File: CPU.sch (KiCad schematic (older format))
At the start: 13 parts, among them P8 SWD, U1 STM32F40X_LQFP64, Y1 Crystal

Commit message: - removed lots of unused circuitry - implemented new DMOS power stage - power supplies still missing - removed rescue lib and fixed referenced
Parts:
- removed C17, C22: 15p, Capacitor_SMD:C_0805_2012Metric, symbol Revolter-rescue:C-RESCUE-BLDC_4
- removed U1: STM32F40X_LQFP64, Package_QFP:LQFP-64_10x10mm_P0.5mm, symbol Revolter-rescue:STM32F40X_LQFP64
- removed Y1: Crystal, Crystal:Crystal_HC49-U_Vertical, symbol Device:Crystal
- added C1, C3: 15p, symbol Device:C_Small
- added C4: 1u, Capacitor_SMD:C_0805_2012Metric, symbol Device:C
- added L1: 100u, symbol pspice:INDUCTOR
- added U1: STM32F405RGTx, Package_QFP:LQFP-64_10x10mm_P0.5mm, symbol MCU_ST_STM32F4:STM32F405RGTx
- added Y1: 8MHz, symbol Device:Crystal_Small
- C18, C19, C20, C21, C23, C24, C25, C26: symbol Revolter-rescue:C-RESCUE-BLDC_4 -> Device:C
- P8: symbol Revolter-rescue:CONN_6 -> Connector_Generic:Conn_01x06
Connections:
- net labels added: CURRENT_U, CURRENT_V, CURRENT_W, HALL_U, HALL_V, HALL_W, HU, HV, HW, LU, LV, LW, VOLTAGE_U, VOLTAGE_V, VOLTAGE_W
- net labels removed: CURRENT_1, CURRENT_2, CURRENT_3, H1, H2, H3, HALL_1, HALL_2, HALL_3, L1, L2, L3, SERVO, VOLTAGE_1, VOLTAGE_2, VOLTAGE_3
- wire segments 69 -> 19
- no-connect marks 17 -> 20
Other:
- note removed: "Bypass, place next to VDD pins"
- note removed: "Required for USB\nto work"
- note removed: "Reset pin internally\npulled up"

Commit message: - fixed ACS730 pin issue - added power supplies - added footprint library - added footprint for IRSM005
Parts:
- removed Y1: 8MHz, symbol Device:Crystal_Small
- added Y1: 8MHz, Crystal:Crystal_SMD_3225-4Pin_3.2x2.5mm, symbol Device:Crystal_GND24
- C1, C3: footprint (none) -> Capacitor_SMD:C_0805_2012Metric
- L1: footprint (none) -> Inductor_SMD:L_0805_2012Metric
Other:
- moved on the sheet: C1, C3
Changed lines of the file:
@@
 F 0 "L1" V 5954 1328 50  0000 L CNN
 F 1 "100u" V 6045 1328 50  0000 L CNN
-F 2 "" H 6000 1250 50  0001 C CNN
+F 2 "Inductor_SMD:L_0805_2012Metric" H 6000 1250 50  0001 C CNN
 F 3 "~" H 6000 1250 50  0001 C CNN
 	1    6000 1250
@@
 	4900 1700 4750 1700
 $Comp
-L Device:Crystal_Small Y1
-U 1 1 5EE66624
-P 4000 2900
-F 0 "Y1" H 4000 3125 50  0000 C CNN
-F 1 "8MHz" H 4000 3034 50  0000 C CNN
-F 2 "" H 4000 2900 50  0001 C CNN
-F 3 "~" H 4000 2900 50  0001 C CNN
-	1    4000 2900
-	1    0    0    -1
-$EndComp
-Wire Wire Line
-	4100 2900 5000 2900
-Wire Wire Line
-	5000 3000 3900 3000
-Wire Wire Line
-	3900 3000 3900 2900
-$Comp
 L Device:C_Small C1
 U 1 1 5EE68BFE
-P 3900 3150
-F 0 "C1" H 3808 3104 50  0000 R CNN
-F 1 "15p" H 3808 3195 50  0000 R CNN
-F 2 "" H 3900 3150 50  0001 C CNN
-F 3 "~" H 3900 3150 50  0001 C CNN
-	1    3900 3150
+P 3750 3200
+F 0 "C1" H 3658 3154 50  0000 R CNN
+F 1 "15p" H 3658 3245 50  0000 R CNN
+F 2 "Capacitor_SMD:C_0805_2012Metric" H 3750 3200 50  0001 C CNN
+F 3 "~" H 3750 3200 50  0001 C CNN
+	1    3750 3200
 	1    0    0    1
 $EndComp
@@
 L Device:C_Small C3
 U 1 1 5EE6B932
-P 4100 3150
-F 0 "C3" H 4008 3196 50  0000 R CNN
-F 1 "15p" H 4008 3105 50  0000 R CNN
-F 2 "" H 4100 3150 50  0001 C CNN
-F 3 "~" H 4100 3150 50  0001 C CNN
-	1    4100 3150
+P 4050 3200
+F 0 "C3" H 3958 3246 50  0000 R CNN
+F 1 "15p" H 3958 3155 50  0000 R CNN
+F 2 "Capacitor_SMD:C_0805_2012Metric" H 4050 3200 50  0001 C CNN
+F 3 "~" H 4050 3200 50  0001 C CNN
+	1    4050 3200
 	-1   0    0    -1
 $EndComp
 Wire Wire Line
-	4100 3050 4100 2900
-Connection ~ 4100 2900
-Wire Wire Line
-	3900 3000 3900 3050
-Connection ~ 3900 3000
+	4050 3100 4050 2900
+Wire Wire Line
+	3750 3000 3750 3100
 $Comp
 L power:GND #PWR0114
 U 1 1 5EE6D37C
-P 3900 3250
-F 0 "#PWR0114" H 3900 3000 50  0001 C CNN
-F 1 "GND" H 3905 3077 50  0000 C CNN
-F 2 "" H 3900 3250 50  0001 C CNN
-F 3 "" H 3900 3250 50  0001 C CNN
-	1    3900 3250
+P 3750 3300
+F 0 "#PWR0114" H 3750 3050 50  0001 C CNN
+F 1 "GND" H 3755 3127 50  0000 C CNN
+F 2 "" H 3750 3300 50  0001 C CNN
+F 3 "" H 3750 3300 50  0001 C CNN
+	1    3750 3300
 	1    0    0    -1
 $EndComp
@@
 L power:GND #PWR0115
 U 1 1 5EE6E0B7
-P 4100 3250
-F 0 "#PWR0115" H 4100 3000 50  0001 C CNN
-F 1 "GND" H 4105 3077 50  0000 C CNN
-F 2 "" H 4100 3250 50  0001 C CNN
-F 3 "" H 4100 3250 50  0001 C CNN
-	1    4100 3250
+P 4050 3300
+F 0 "#PWR0115" H 4050 3050 50  0001 C CNN
+F 1 "GND" H 4055 3127 50  0000 C CNN
+F 2 "" H 4050 3300 50  0001 C CNN
+F 3 "" H 4050 3300 50  0001 C CNN
+	1    4050 3300
 	1    0    0    -1
 $EndComp
@@
 NoConn ~ 5000 4900
 NoConn ~ 5000 3200
+$Comp
+L Device:Crystal_GND24 Y1
+U 1 1 5EF3EE13
+P 3900 2900
+F 0 "Y1" H 4094 2946 50  0000 L CNN
+F 1 "8MHz" H 4094 2855 50  0000 L CNN
+F 2 "Crystal:Crystal_SMD_3225-4Pin_3.2x2.5mm" H 3900 2900 50  0001 C CNN
+F 3 "~" H 3900 2900 50  0001 C CNN
+	1    3900 2900
+	1    0    0    -1
+$EndComp
+Wire Wire Line
+	4050 2900 5000 2900
+Wire Wire Line
+	5000 3000 3750 3000
+Wire Wire Line
+	3750 3000 3750 2900
+Connection ~ 3750 3000
+Connection ~ 4050 2900
+$Comp
+L power:GND #PWR0177
+U 1 1 5EF48D07
+P 3900 3100
+F 0 "#PWR0177" H 3900 2850 50  0001 C CNN
+F 1 "GND" H 3905 2927 50  0000 C CNN
+F 2 "" H 3900 3100 50  0001 C CNN
+F 3 "" H 3900 3100 50  0001 C CNN
+	1    3900 3100
+	1    0    0    -1
+$EndComp
+$Comp
+L power:GND #PWR0178
+U 1 1 5EF4921F
+P 3900 2700
+F 0 "#PWR0178" H 3900 2450 50  0001 C CNN
+F 1 "GND" H 3905 2527 50  0000 C CNN
+F 2 "" H 3900 2700 50  0001 C CNN
+F 3 "" H 3900 2700 50  0001 C CNN
+	1    3900 2700
+	-1   0    0    1
+$EndComp
 $EndSCHEMATC

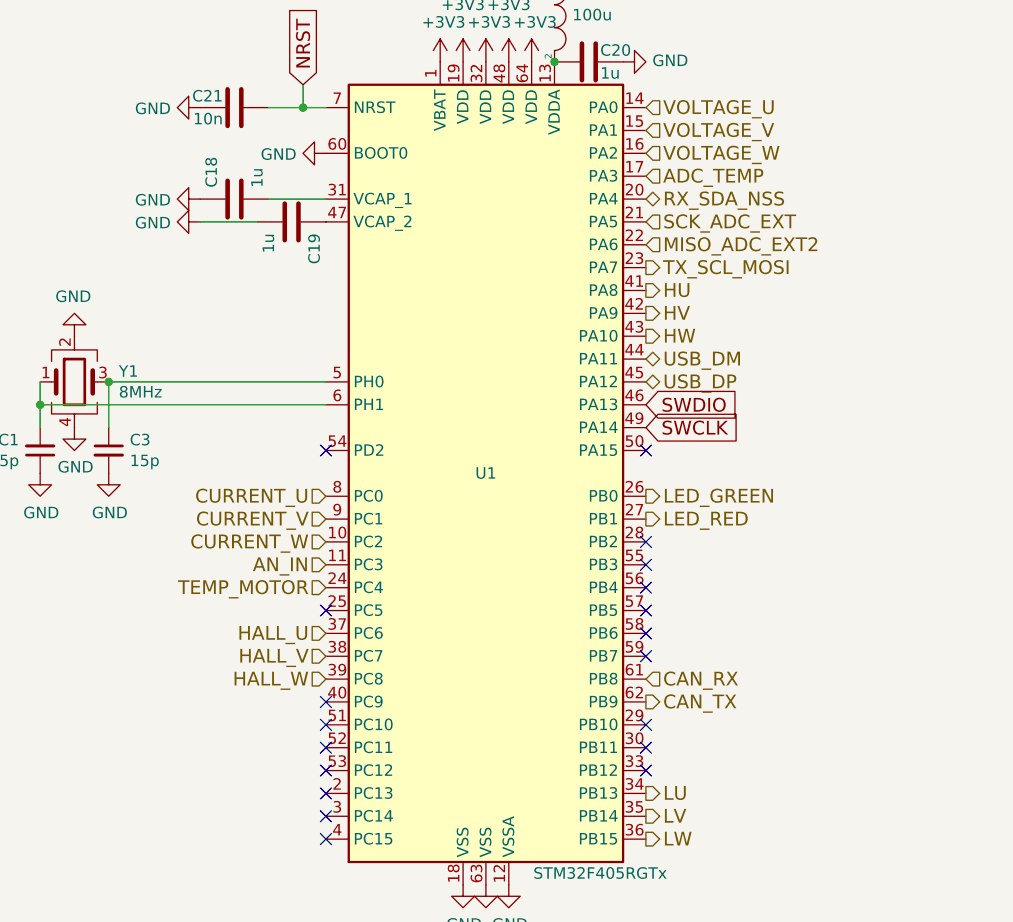
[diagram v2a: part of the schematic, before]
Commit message: - added temp sensors and fan/pump outputs - made footprint selection
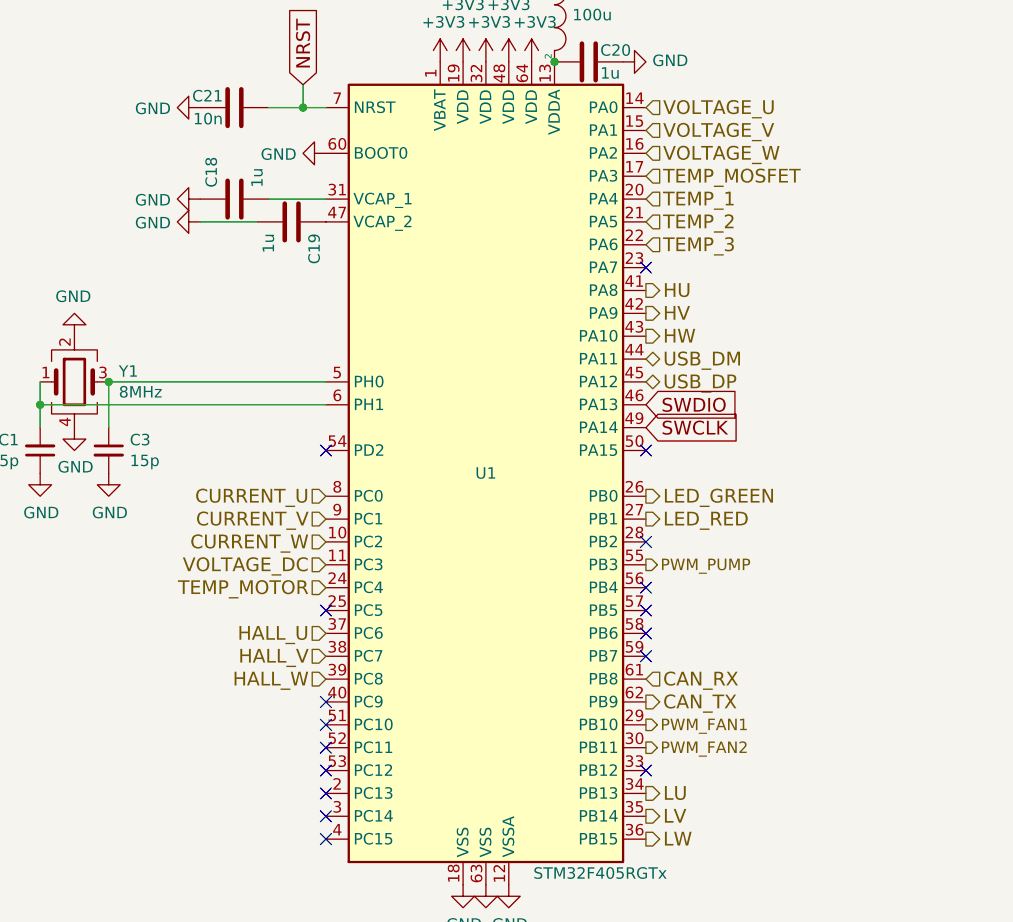
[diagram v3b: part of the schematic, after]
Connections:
- net labels added: PWM_FAN1, PWM_FAN2, PWM_PUMP, TEMP_1, TEMP_2, TEMP_3, TEMP_MOSFET, VOLTAGE_DC
- net labels removed: ADC_TEMP, AN_IN, MISO_ADC_EXT2, RX_SDA_NSS, SCK_ADC_EXT, TX_SCL_MOSI
- no-connect marks 20 -> 18
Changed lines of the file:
@@
 $Descr A4 11693 8268
 encoding utf-8
-Sheet 2 4
+Sheet 4 4
 Title "HSWR CPU"
 Date "2017-02-05"
@@
 LU
 Text HLabel 6400 2200 2    60   Input ~ 0
-SCK_ADC_EXT
+TEMP_2
 Text HLabel 6400 2500 2    60   Output ~ 0
 HU
@@
 CURRENT_U
 Text HLabel 5000 3700 0    60   Input ~ 0
-AN_IN
+VOLTAGE_DC
 Wire Notes Line
 	9250 2650 9250 3550
@@
 LED_GREEN
 Text HLabel 6400 2300 2    60   Input ~ 0
-MISO_ADC_EXT2
-Text HLabel 6400 2400 2    60   Output ~ 0
-TX_SCL_MOSI
+TEMP_3
 Text HLabel 6400 2000 2    60   Input ~ 0
-ADC_TEMP
-Text HLabel 6400 2100 2    60   3State ~ 0
-RX_SDA_NSS
+TEMP_MOSFET
+Text HLabel 6400 2100 2    60   Input ~ 0
+TEMP_1
 $Comp
 L power:+3V3 #PWR050
@@
 HALL_W
 $Comp
-L MCU_ST_STM32F4:STM32F405RGTx U1
-U 1 1 5EE38B5C
-P 5700 3300
-F 0 "U1" H 5700 3300 50  0000 C CNN
-F 1 "STM32F405RGTx" H 6200 1550 50  0000 C CNN
-F 2 "Package_QFP:LQFP-64_10x10mm_P0.5mm" H 5100 1600 50  0001 R CNN
-F 3 "http://www.st.com/st-web-ui/static/active/en/resource/technical/document/datasheet/DM00037051.pdf" H 5700 3300 50  0001 C CNN
-	1    5700 3300
-	1    0    0    -1
-$EndComp
-$Comp
 L power:GND #PWR0101
 U 1 1 5EE3F753
@@
 	0    -1   -1   0
 $EndComp
-Connection ~ 6000 1500
 Wire Wire Line
 	4750 2100 5000 2100
@@
 	0    1    1    0
 $EndComp
-NoConn ~ 6400 3700
 NoConn ~ 6400 3800
 NoConn ~ 6400 3900
 NoConn ~ 6400 4000
 NoConn ~ 6400 4100
-NoConn ~ 6400 4400
-NoConn ~ 6400 4500
 NoConn ~ 6400 4600
 NoConn ~ 5000 3900
@@
 	-1   0    0    1
 $EndComp
+Connection ~ 6000 1500
+$Comp
+L MCU_ST_STM32F4:STM32F405RGTx U1
+U 1 1 5EE38B5C
+P 5700 3300
+F 0 "U1" H 5700 3300 50  0000 C CNN
+F 1 "STM32F405RGTx" H 6200 1550 50  0000 C CNN
+F 2 "Package_QFP:LQFP-64_10x10mm_P0.5mm" H 5100 1600 50  0001 R CNN
+F 3 "http://www.st.com/st-web-ui/static/active/en/resource/technical/document/datasheet/DM00037051.pdf" H 5700 3300 50  0001 C CNN
+	1    5700 3300
+	1    0    0    -1
+$EndComp
+Text HLabel 6400 3700 2    50   Output ~ 0
+PWM_PUMP
+NoConn ~ 6400 2400
+Text HLabel 6400 4400 2    50   Output ~ 0
+PWM_FAN1
+Text HLabel 6400 4500 2    50   Output ~ 0
+PWM_FAN2
 $EndSCHEMATC

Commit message: - did most of the layout
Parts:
- removed C26: 1u, Capacitor_SMD:C_0805_2012Metric, symbol Device:C
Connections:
- wire segments 19 -> 17
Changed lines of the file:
@@
 	-1   0    0    1
 $EndComp
-$Comp
-L Device:C C26
-U 1 1 53F7744E
-P 10100 1300
-AR Path="/53F7744E" Ref="C26"  Part="1"
-AR Path="/5899E230/53F7744E" Ref="C26"  Part="1"
-F 0 "C26" H 10150 1400 50  0000 L CNN
-F 1 "1u" H 10150 1200 50  0000 L CNN
-F 2 "Capacitor_SMD:C_0805_2012Metric" H 10100 1300 60  0001 C CNN
-F 3 "" H 10100 1300 60  0001 C CNN
-	1    10100 1300
-	-1   0    0    1
-$EndComp
-Connection ~ 9900 1450
 Connection ~ 9700 1450
 Connection ~ 9700 1150
-Connection ~ 9900 1150
 Wire Wire Line
 	9750 3100 9600 3100
@@
 $EndComp
 Wire Wire Line
-	9900 1450 10100 1450
-Wire Wire Line
 	9500 1450 9700 1450
 Wire Wire Line
 	9500 1150 9700 1150
-Wire Wire Line
-	9900 1150 10100 1150
 Text HLabel 5000 3500 0    60   Input ~ 0
 CURRENT_V

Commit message: - shrink PCB to 50x50mm
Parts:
- removed C21: 10n, Capacitor_SMD:C_0805_2012Metric, symbol Device:C
- removed P8: SWD, Connector_PinHeader_2.54mm:PinHeader_2x03_P2.54mm_Vertical, symbol Connector_Generic:Conn_01x06
- added J4: Conn_01x03_Male, Connector_PinHeader_2.00mm:PinHeader_1x03_P2.00mm_Vertical, symbol Connector:Conn_01x03_Male
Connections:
- net labels removed: NRST
- wire segments 17 -> 13
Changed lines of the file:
@@
 $EndComp
 $Comp
-L Device:C C21
-U 1 1 53F75896
-P 4600 1700
-AR Path="/53F75896" Ref="C21"  Part="1"
-AR Path="/5899E230/53F75896" Ref="C21"  Part="1"
-F 0 "C21" V 4650 1750 50  0000 L CNN
-F 1 "10n" V 4550 1750 50  0000 L CNN
-F 2 "Capacitor_SMD:C_0805_2012Metric" H 4600 1700 60  0001 C CNN
-F 3 "" H 4600 1700 60  0001 C CNN
-	1    4600 1700
-	0    -1   -1   0
-$EndComp
-$Comp
-L Connector_Generic:Conn_01x06 P8
-U 1 1 53F77410
-P 9950 3100
-F 0 "P8" V 10050 3100 60  0000 C CNN
-F 1 "SWD" H 9950 3450 60  0000 C CNN
-F 2 "Connector_PinHeader_2.54mm:PinHeader_2x03_P2.54mm_Vertical" H 9950 3100 60  0001 C CNN
-F 3 "" H 9950 3100 60  0001 C CNN
-	1    9950 3100
-	1    0    0    -1
-$EndComp
-$Comp
 L power:GND #PWR044
 U 1 1 53F7741D
-P 9600 3100
-F 0 "#PWR044" H 9600 3100 30  0001 C CNN
-F 1 "GND" H 9600 3030 30  0001 C CNN
-F 2 "" H 9600 3100 60  0001 C CNN
-F 3 "" H 9600 3100 60  0001 C CNN
-	1    9600 3100
+P 9750 3200
+F 0 "#PWR044" H 9750 3200 30  0001 C CNN
+F 1 "GND" H 9750 3130 30  0001 C CNN
+F 2 "" H 9750 3200 60  0001 C CNN
+F 3 "" H 9750 3200 60  0001 C CNN
+	1    9750 3200
 	0    1    1    0
 $EndComp
 Text GLabel 9750 3000 0    60   Input ~ 0
 SWCLK
-Text GLabel 9750 3200 0    60   Input ~ 0
+Text GLabel 9750 3100 0    60   Input ~ 0
 SWDIO
-Text GLabel 9750 3300 0    60   Input ~ 0
-NRST
 $Comp
 L Device:C C23
@@
 Connection ~ 9700 1450
 Connection ~ 9700 1150
-Wire Wire Line
-	9750 3100 9600 3100
-NoConn ~ 9750 3400
 Text HLabel 6400 2800 2    60   BiDi ~ 0
 USB_DM
@@
 Text Notes 9250 3750 0    60   ~ 0
 Programming / Debug\nconnector
-Text GLabel 4900 1600 1    60   Input ~ 0
-NRST
 $Bitmap
 Pos 1750 6700
@@
 TEMP_1
 $Comp
-L power:+3V3 #PWR050
-U 1 1 5752A907
-P 9750 2900
-F 0 "#PWR050" H 9750 2750 50  0001 C CNN
-F 1 "+3V3" V 9750 3150 50  0000 C CNN
-F 2 "" H 9750 2900 50  0000 C CNN
-F 3 "" H 9750 2900 50  0000 C CNN
-	1    9750 2900
-	0    -1   -1   0
-$EndComp
-$Comp
 L power:+3V3 #PWR051
 U 1 1 5752A9C6
@@
 SWCLK
 $Comp
-L power:GND #PWR0113
-U 1 1 5EE5E816
-P 4450 1700
-F 0 "#PWR0113" H 4450 1450 50  0001 C CNN
-F 1 "GND" V 4455 1572 50  0000 R CNN
-F 2 "" H 4450 1700 50  0001 C CNN
-F 3 "" H 4450 1700 50  0001 C CNN
-	1    4450 1700
-	0    1    1    0
-$EndComp
-Wire Wire Line
-	5000 1700 4900 1700
-Wire Wire Line
-	4900 1600 4900 1700
-Connection ~ 4900 1700
-Wire Wire Line
-	4900 1700 4750 1700
-$Comp
 L Device:C_Small C1
 U 1 1 5EE68BFE
@@
 Text HLabel 6400 4500 2    50   Output ~ 0
 PWM_FAN2
+Connection ~ 9500 1150
+Connection ~ 9500 1450
+$Comp
+L Connector:Conn_01x03_Male J4
+U 1 1 5FAC96B0
+P 9950 3100
+F 0 "J4" H 9922 3124 50  0000 R CNN
+F 1 "Conn_01x03_Male" H 9922 3033 50  0000 R CNN
+F 2 "Connector_PinHeader_2.00mm:PinHeader_1x03_P2.00mm_Vertical" H 9950 3100 50  0001 C CNN
+F 3 "~" H 9950 3100 50  0001 C CNN
+	1    9950 3100
+	-1   0    0    -1
+$EndComp
+NoConn ~ 5000 1700
 $EndSCHEMATC
